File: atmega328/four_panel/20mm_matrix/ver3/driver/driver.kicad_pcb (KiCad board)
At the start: 2 copper layers, 40 x 40 mm, 56 parts, among them IC1 ATMEGA328P-M, IC2 ATMEGA328P-M, IC3 ATMEGA328P-M, IC4 ATMEGA328P-M, P1 CONN_2X2, P2 CONN_2X2, P3 CONN_2X2, P4 CONN_2X2, X1 CER_RESO, X2 CER_RESO, X3 CER_RESO, X4 CER_RESO

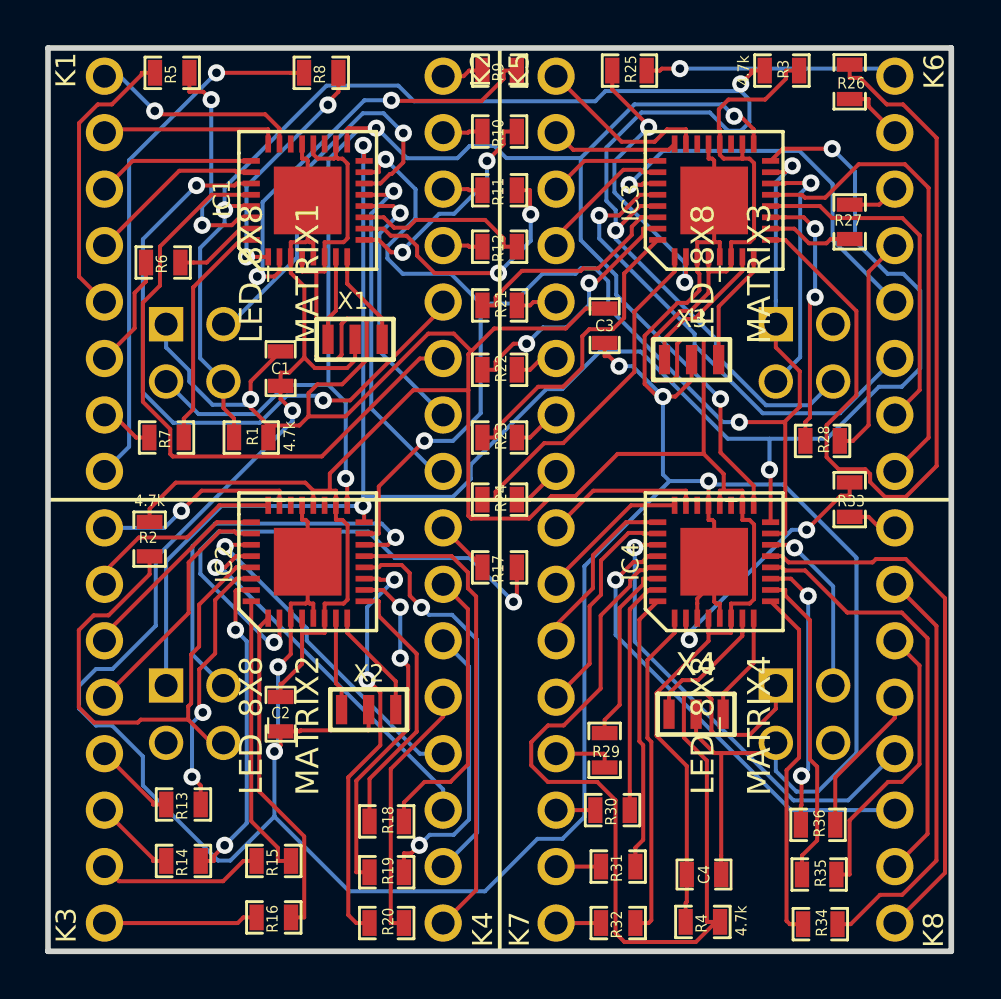
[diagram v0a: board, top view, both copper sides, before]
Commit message: Re-routed driver so that there are no traces going through the clocks.
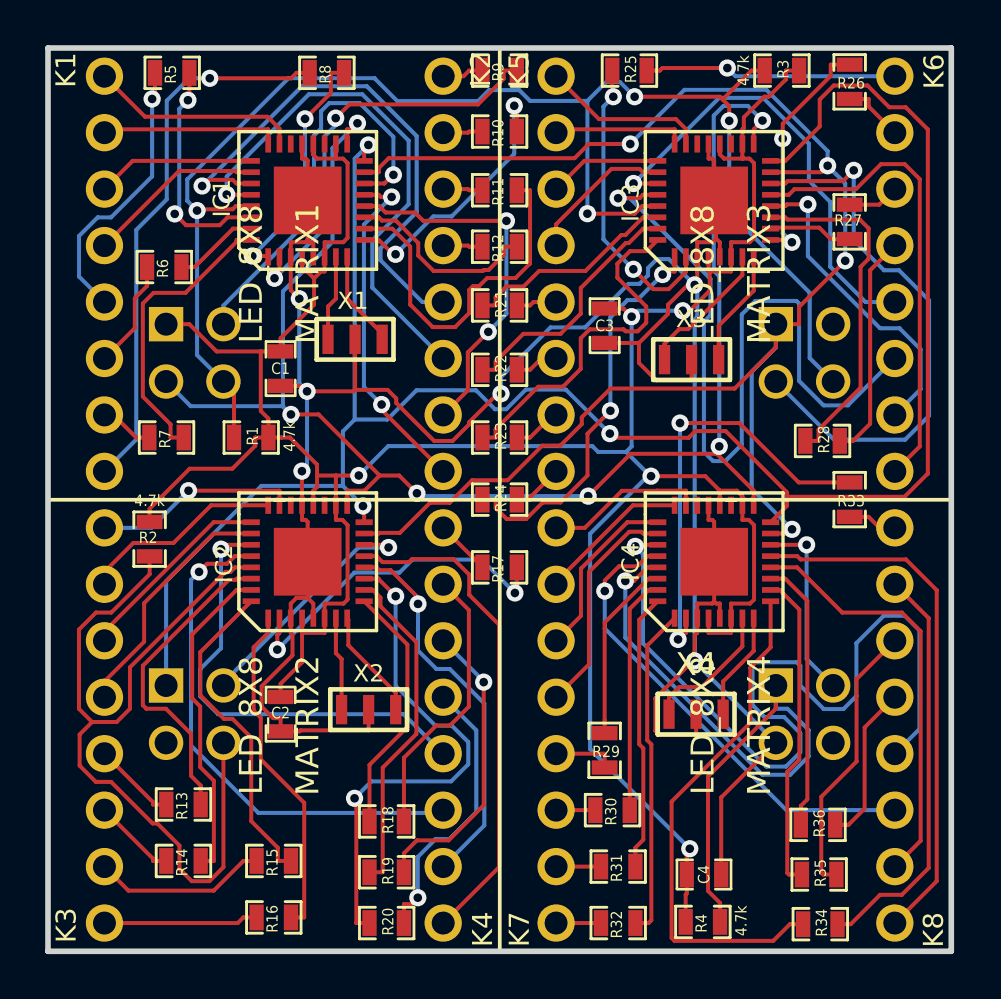
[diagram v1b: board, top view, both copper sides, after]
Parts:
- moved R8 0.25 mm to (62.4, 51.1)
- moved R6 0.21 mm to (55.1, 59.7)
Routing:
- net GND: track 171.5 -> 124.3 mm
- net +5V: track 160.6 -> 128.6 mm, vias 1 -> 5
- net /COL5_DRV2: track 38.6 -> 10.7 mm, vias 0 -> 2
- net /ROW4_DRV3: track 20.5 -> 38.3 mm
- net /RESET_DRV3: track 45.3 -> 31.1 mm, vias 0 -> 1
- net /CS2: track 11.2 -> 24.9 mm
- net /RESET_DRV1: track 23.8 -> 37.2 mm
- net /ROW5_DRV2: track 21.6 -> 34.9 mm
- net /COL4_DRV1: track 23.8 -> 15.4 mm
- net /MOSI: track 61.8 -> 69.9 mm
- net /COL4_DRV3: track 11.5 -> 19.3 mm
- net /COL5_DRV3: track 15.7 -> 22.9 mm
- net /CS1: track 17.9 -> 11.0 mm
- net /MISO: track 81.6 -> 88.4 mm, vias 4 -> 3
- net /ROW5_DRV1: track 16.8 -> 22.9 mm
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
